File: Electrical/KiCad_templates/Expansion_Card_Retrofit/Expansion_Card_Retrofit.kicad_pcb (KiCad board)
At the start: 4 copper layers, 70 x 75 mm, 386 parts, among them J1 Conn 10P, P1 USB_C_Plug_USB2.0, Q1 DMG1012T, Q2 Q_PMOS_SGD, Q3 Q_Dual_NPN_NPN_C2E2C1E1B1B2, U1 AP7366EA-3.3, U2 RP2040, U3 W25Q16JVUXIQ, U4 RP2040, U5 W25Q16JVUXIQ, X1 SX2M12.000M20F30TNN

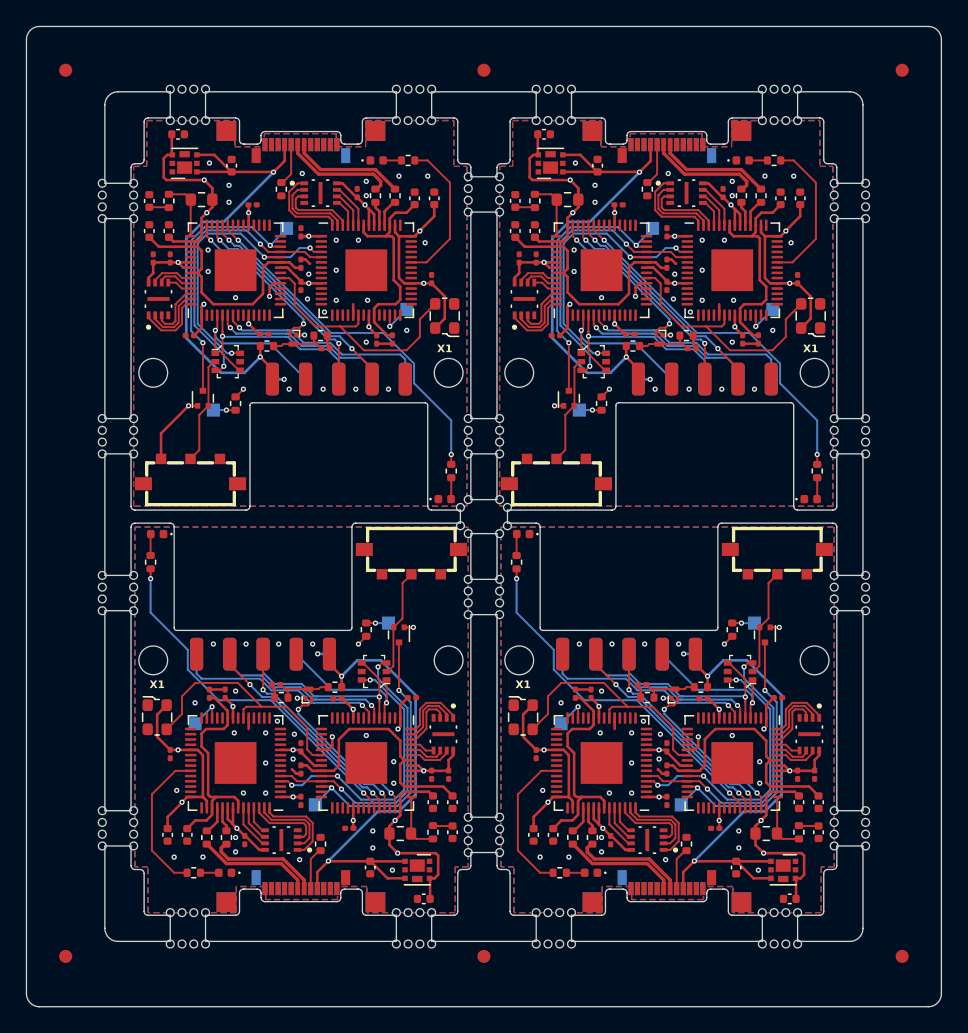
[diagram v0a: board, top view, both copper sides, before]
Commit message: Fixed missing drill holes for switch
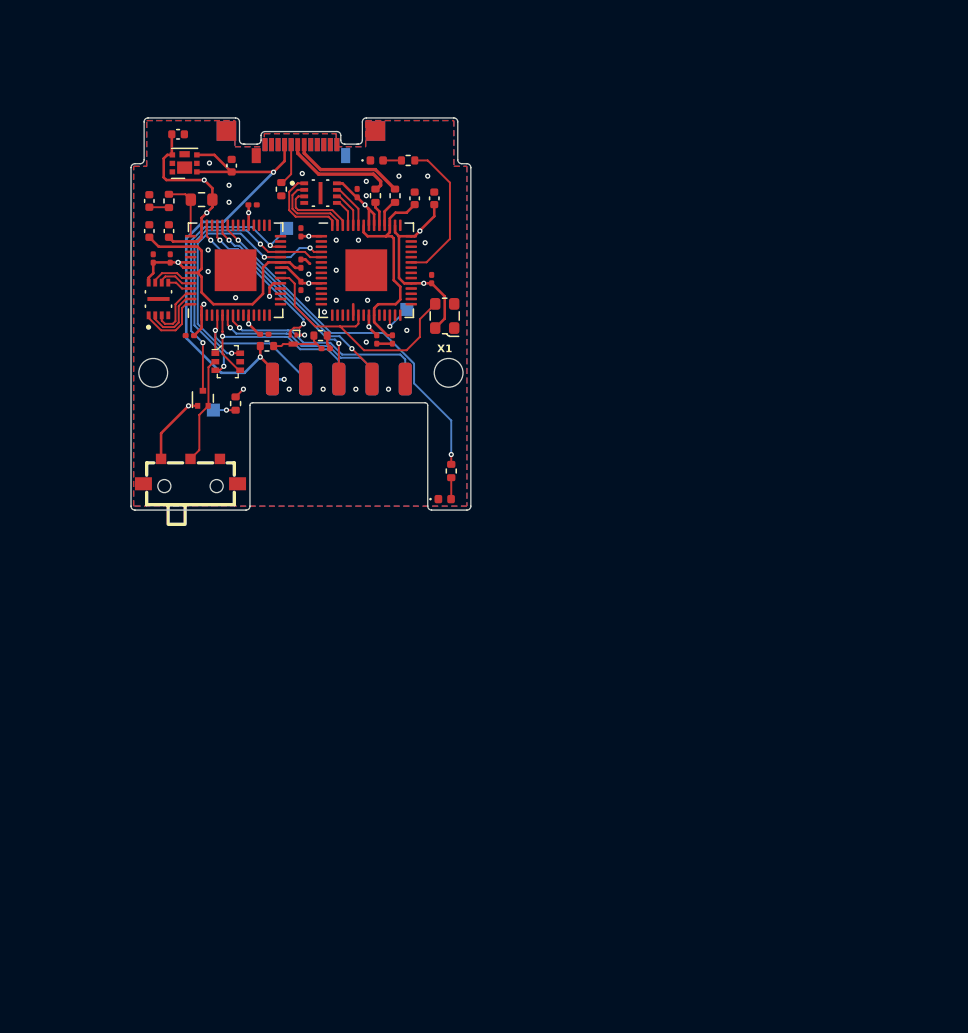
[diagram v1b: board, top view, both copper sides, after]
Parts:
- removed the C1 at (154.3, 132.3)
- removed the C1 at (126.3, 132.3)
- removed the C1 at (143.7, 78.7)
- removed the C10 at (140.5, 91.7)
- removed the C10 at (129.5, 119.3)
- removed the C10 at (157.5, 119.3)
- removed the C11 at (132.3, 125.2)
- removed the C11 at (160.3, 125.2)
- removed the C11 at (137.7, 85.8)
- removed the C12 at (142.0, 119.0)
- removed the C12 at (114.0, 119.0)
- removed the C12 at (156.0, 92.0)
- removed the C13 at (144.7, 130.2)
- removed the C13 at (116.7, 130.2)
- removed the C13 at (153.3, 80.8)
- removed the C14 at (112.3, 129.8)
- removed the C14 at (140.3, 129.8)
- removed the C14 at (157.7, 81.2)
- removed the C15 at (138.8, 129.8)
- removed the C15 at (110.8, 129.8)
- removed the C15 at (159.2, 81.2)
- removed the C16 at (149.0, 83.8)
- removed the C16 at (121.0, 127.2)
- removed the C16 at (149.0, 127.2)
- removed the C18 at (119.1, 118.3)
- removed the C18 at (150.9, 92.7)
- removed the C18 at (147.1, 118.3)
- removed the C19 at (149.0, 123.2)
- removed the C19 at (149.0, 87.8)
- removed the C19 at (121.0, 123.2)
- removed the C2 at (130.4, 134.8)
- removed the C2 at (139.6, 76.2)
- removed the C2 at (158.4, 134.8)
- removed the C20 at (154.8, 92.0)
- removed the C20 at (115.2, 119.0)
- removed the C20 at (143.2, 119.0)
- removed the C21 at (111.0, 123.7)
- removed the C21 at (139.0, 123.7)
- removed the C21 at (159.0, 87.3)
- removed the C22 at (146.2, 91.5)
- removed the C22 at (151.8, 119.5)
- removed the C22 at (123.8, 119.5)
- removed the C24 at (124.7, 129.3)
- removed the C24 at (152.7, 129.3)
- removed the C24 at (145.3, 81.7)
- removed the C5 at (149.0, 86.2)
- removed the C5 at (121.0, 124.8)
- removed the C5 at (149.0, 124.8)
- removed the C6 at (131.0, 125.2)
- removed the C6 at (159.0, 125.2)
- removed the C6 at (139.0, 85.8)
- removed the C7 at (132.6, 127.3)
- removed the C7 at (160.6, 127.3)
- removed the C7 at (137.4, 83.7)
- removed the C8 at (159.1, 127.3)
- removed the C8 at (138.9, 83.7)
- removed the C8 at (131.1, 127.3)
- removed the C9 at (132.6, 129.7)
- removed the C9 at (137.4, 81.3)
- removed the C9 at (160.6, 129.7)
- removed the D1 at (110.0, 106.8)
- removed the D1 at (138.0, 106.8)
- removed the D1 at (160.0, 104.2)
- removed the D2 at (115.2, 132.8)
- removed the D2 at (143.2, 132.8)
- removed the D2 at (154.8, 78.2)
- removed the H1 at (160.3, 116.5)
- removed the H1 at (132.3, 116.5)
- removed the H1 at (137.7, 94.5)
- removed the H2 at (137.7, 116.5)
- removed the H2 at (160.3, 94.5)
- removed the H2 at (109.7, 116.5)
- removed the J1 at (151.9, 101.2)
- removed the J1 at (146.1, 109.8)
- removed the J1 at (118.1, 109.8)
- removed the P1 at (149.0, 77.0)
- removed the P1 at (149.0, 134.0)
- removed the P1 at (121.0, 134.0)
- removed the Q1 at (148.4, 92.0)
- removed the Q1 at (149.6, 119.0)
- removed the Q1 at (121.6, 119.0)
- removed the Q2 at (141.5, 96.5)
- removed the Q2 at (156.5, 114.5)
- removed the Q2 at (128.5, 114.5)
- removed the Q3 at (154.6, 117.3)
- removed the Q3 at (126.6, 117.3)
- removed the Q3 at (143.4, 93.7)
- removed the R1 at (147.5, 80.5)
- removed the R1 at (150.5, 130.6)
- removed the R1 at (122.5, 130.6)
- removed the R10 at (113.8, 130.1)
- removed the R10 at (141.8, 130.1)
- removed the R10 at (156.2, 81.0)
- removed the R11 at (128.6, 129.8)
- removed the R11 at (156.6, 129.8)
- removed the R11 at (141.4, 81.2)
- removed the R12 at (159.1, 129.7)
- removed the R12 at (131.1, 129.7)
- removed the R12 at (138.9, 81.3)
- removed the R15 at (151.6, 118.5)
- removed the R15 at (146.4, 92.5)
- removed the R15 at (123.6, 118.5)
- removed the R16 at (147.5, 119.3)
- removed the R16 at (119.5, 119.3)
- removed the R16 at (150.5, 91.7)
- removed the R17 at (157.2, 78.2)
- removed the R17 at (112.8, 132.8)
- removed the R17 at (140.8, 132.8)
- removed the R2 at (154.0, 114.2)
- removed the R2 at (126.0, 114.2)
- removed the R2 at (144.0, 96.8)
- removed the R4 at (109.5, 109.0)
- removed the R4 at (137.5, 109.0)
- removed the R4 at (160.5, 102.0)
- removed the R9 at (154.7, 81.0)
- removed the R9 at (115.3, 130.1)
- removed the R9 at (143.3, 130.1)
- removed REF** (x168): DrillHole_0.6mm, MountingHole:DrillHole_0.6mm
- removed REF** (x6): Fiducial, TestPoint:Fiducial
- removed the S1 at (140.6, 102.0)
- removed the S1 at (129.4, 109.0)
- removed the S1 at (157.4, 109.0)
- removed the TP1 at (143.3, 76.0)
- removed the TP1 at (154.7, 135.0)
- removed the TP1 at (126.7, 135.0)
- removed the TP2 at (143.3, 76.0)
- removed the TP2 at (126.7, 135.0)
- removed the TP2 at (154.7, 135.0)
- removed the TP3 at (115.3, 135.0)
- removed the TP3 at (143.3, 135.0)
- removed the TP3 at (154.7, 76.0)
- removed the TP4 at (143.3, 135.0)
- removed the TP4 at (154.7, 76.0)
- removed the TP4 at (115.3, 135.0)
- removed the TP5 at (127.7, 113.7)
- removed the TP5 at (142.3, 97.3)
- removed the TP5 at (155.7, 113.7)
- removed the TP7 at (147.9, 83.5)
- removed the TP7 at (150.1, 127.5)
- removed the TP7 at (122.1, 127.5)
- removed the TP8 at (140.9, 121.3)
- removed the TP8 at (157.1, 89.7)
- removed the TP8 at (112.9, 121.3)
- removed the U1 at (140.1, 78.5)
- removed the U1 at (157.9, 132.5)
- removed the U1 at (129.9, 132.5)
- removed the U2 at (154.0, 124.3)
- removed the U2 at (144.0, 86.7)
- removed the U2 at (126.0, 124.3)
- removed the U3 at (159.9, 122.2)
- removed the U3 at (131.9, 122.2)
- removed the U3 at (138.1, 88.8)
- removed the U4 at (116.0, 124.3)
- removed the U4 at (144.0, 124.3)
- removed the U4 at (154.0, 86.7)
- removed the U5 at (150.5, 80.8)
- removed the U5 at (147.5, 130.2)
- removed the U5 at (119.5, 130.2)
- removed the X1 at (138.0, 120.8)
- removed the X1 at (160.0, 90.2)
- removed the X1 at (110.0, 120.8)
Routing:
- net +3V3: track 237.1 -> 63.0 mm, vias 64 -> 16
- net VBUS: track 154.0 -> 38.5 mm, vias 8 -> 2
- net LED_EN: track 110.9 -> 27.7 mm, vias 8 -> 2
- net SWCLK: track 90.0 -> 22.5 mm, vias 12 -> 3
- net SWDIO: track 88.6 -> 22.1 mm, vias 8 -> 2
- net /Development Board Section/RUN: track 86.3 -> 21.6 mm, vias 8 -> 2
- net OSC_OUT: track 78.4 -> 19.6 mm
- net /Development Board Section/1V1_CORE: track 76.2 -> 19.0 mm
- net GPIO_ADC0: track 68.6 -> 17.1 mm, vias 8 -> 2
- net /Debug Probe Section/1V1_CORE: track 67.6 -> 16.9 mm
- net GPIO5: track 65.4 -> 16.4 mm, vias 4 -> 1
- net GPIO_ADC1: track 65.3 -> 16.3 mm, vias 8 -> 2
- net GPIO3: track 63.7 -> 15.9 mm, vias 4 -> 1
- net GPIO4: track 55.9 -> 14.0 mm, vias 4 -> 1
- net /Development Board Section/GPIO_ADC3: track 51.0 -> 12.7 mm, vias 8 -> 2
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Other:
- board size 70 x 75 mm -> 26 x 30 mm
